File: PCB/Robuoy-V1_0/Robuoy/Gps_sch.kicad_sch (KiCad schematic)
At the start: 4 parts, among them J501 GPS, U4 USBLC6-4SC6

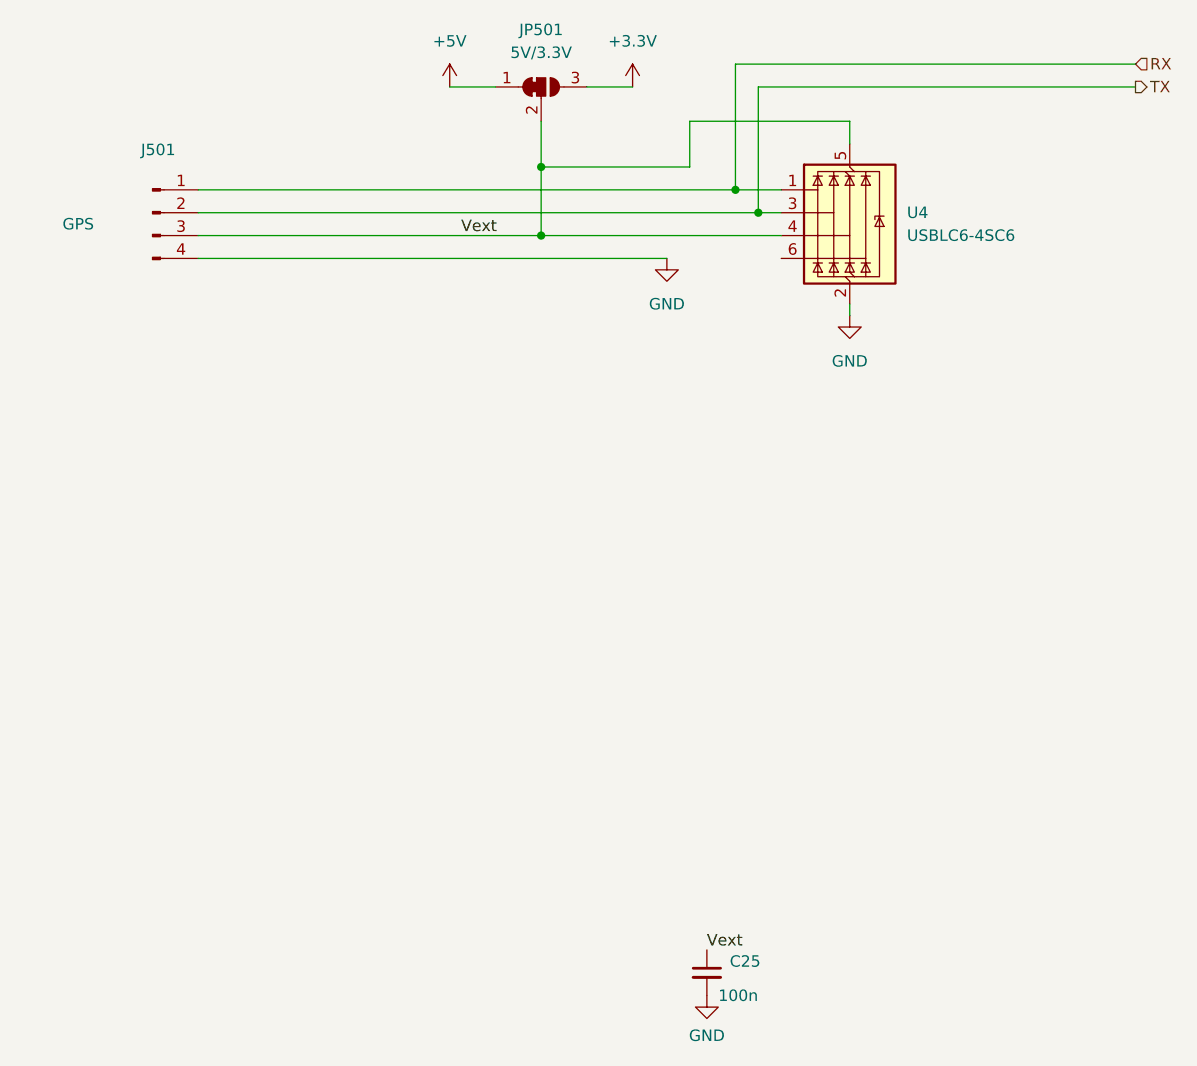
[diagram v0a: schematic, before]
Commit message: Schematics changed for new design
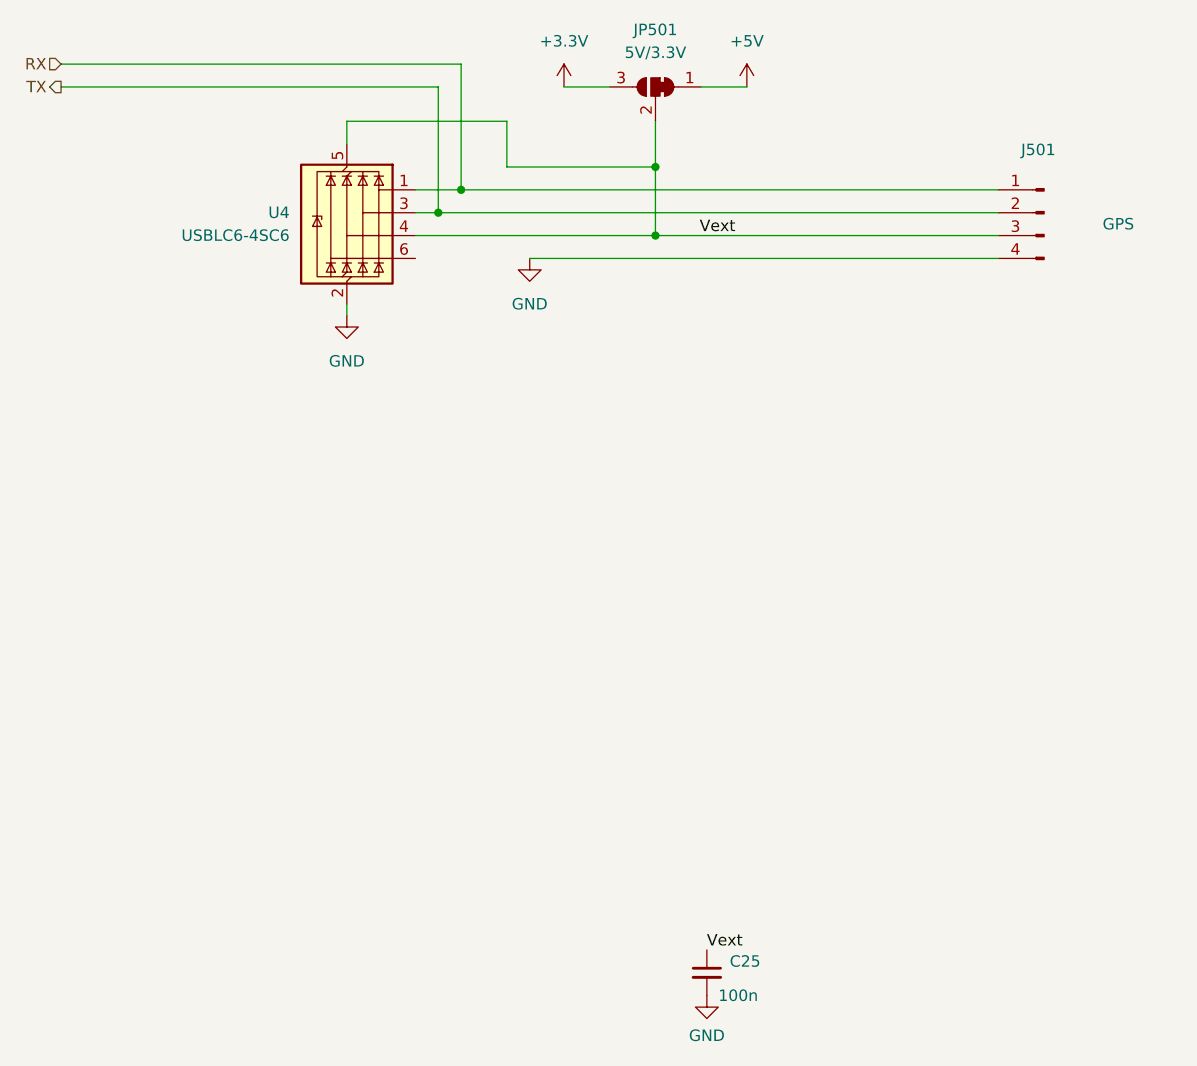
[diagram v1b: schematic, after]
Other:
- moved on the sheet: J501, JP501, U4
